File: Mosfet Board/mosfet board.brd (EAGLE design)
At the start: 50 x 29.2 mm, 26 parts, among them IC1 4081D, U1 MOSFET1, U2 MOSFET2, U3 MOSFET3

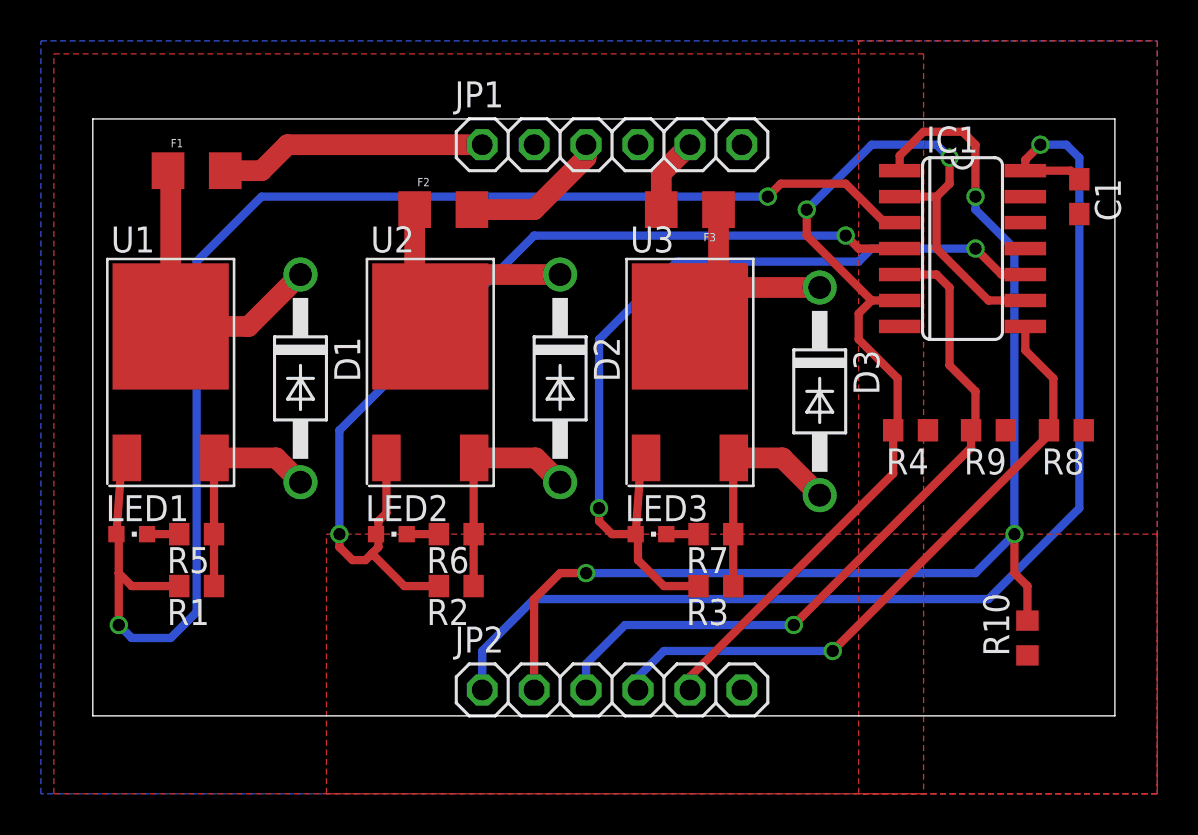
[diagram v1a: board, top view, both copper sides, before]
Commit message: cleaned up silk screens
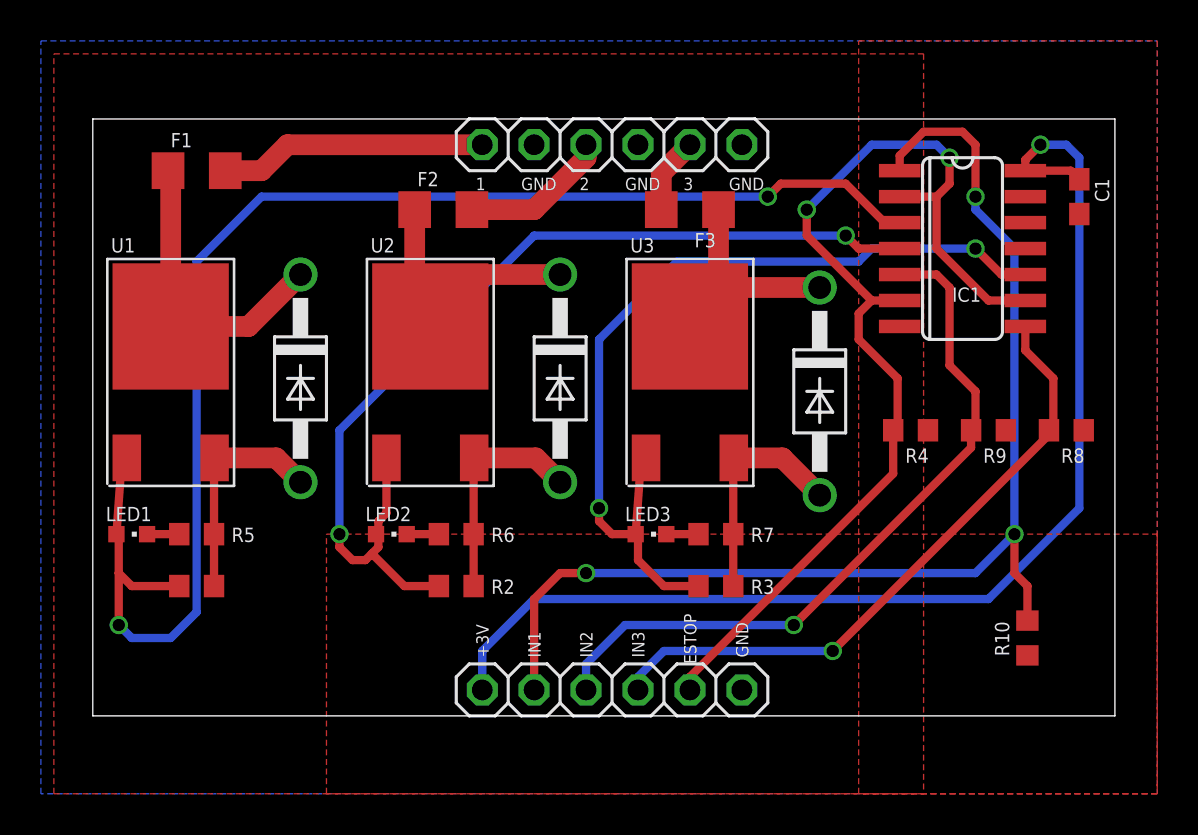
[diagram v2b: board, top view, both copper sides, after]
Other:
- board text added: "+3V"
- board text added: "1"
- board text added: "2"
- board text added: "3"
- board text added: "ESTOP"
- board text added: "GND"
- board text added: "IN1"
- board text added: "IN2"
- board text added: "IN3"
